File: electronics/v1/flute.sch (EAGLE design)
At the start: 45 parts, among them P1 PRESSURE_SENSOR, Q1 BC550C, Q2 BC550C

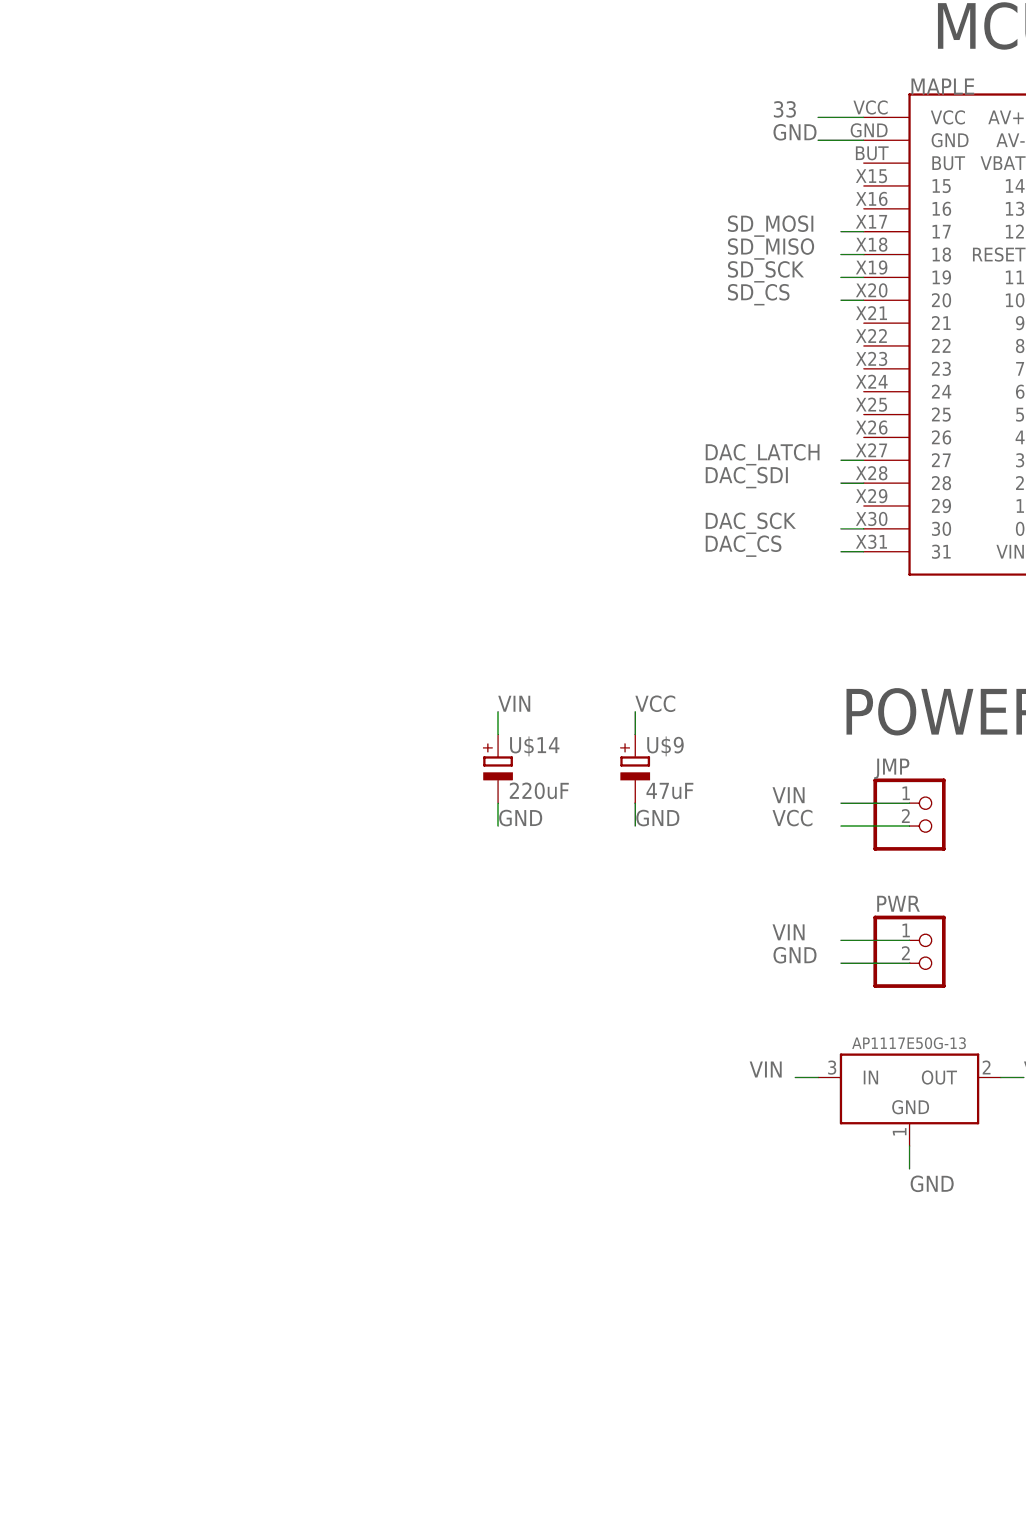
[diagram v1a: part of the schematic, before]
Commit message: Routed V1 (to be checked)
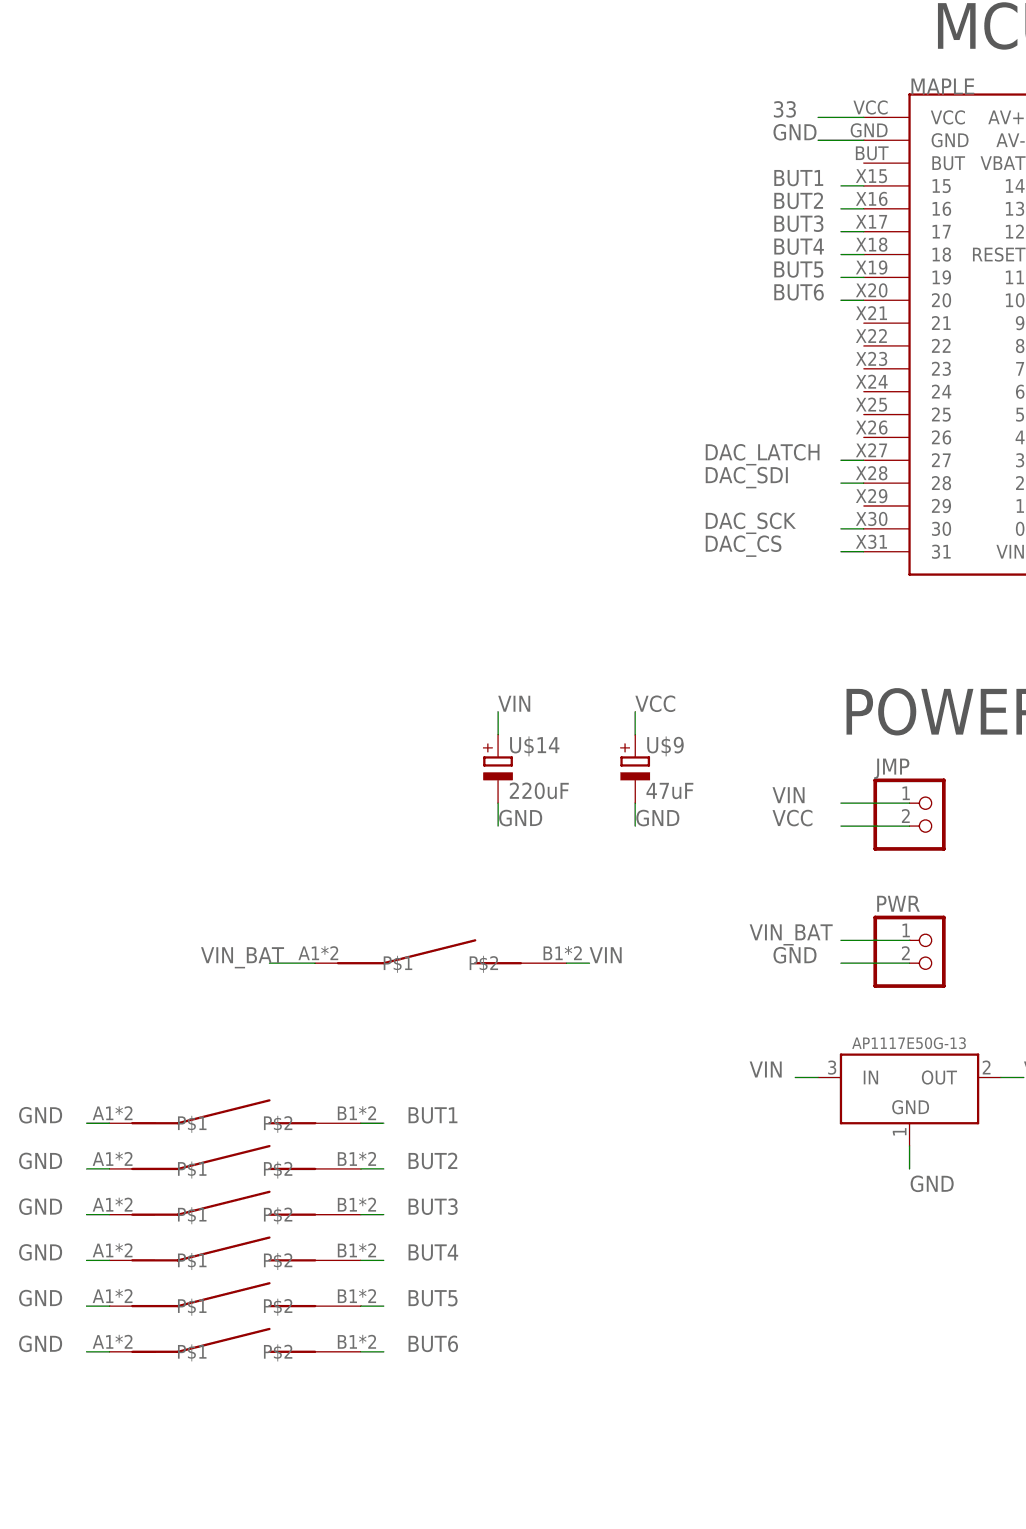
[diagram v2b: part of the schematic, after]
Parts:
- added U$16: SWITCHKCD11, rhoban:SWITCHKCD11
- added U$18, U$19, U$20, U$21, U$22, U$23: SWITCH6X6X10, rhoban:SWITCH6X6X10
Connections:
- removed net SD_CS: MAPLE.20
- removed net SD_MISO: MAPLE.18
- removed net SD_MOSI: MAPLE.17
- removed net SD_SCK: MAPLE.19
- new net BUT1: MAPLE.15, U$18.P$2
- new net BUT2: MAPLE.16, U$19.P$2
- new net BUT3: MAPLE.17, U$20.P$2
- new net BUT4: MAPLE.18, U$21.P$2
- new net BUT5: MAPLE.19, U$22.P$2
- new net BUT6: MAPLE.20, U$23.P$2
- new net VIN_BAT: PWR.1, U$16.P$1
- net GND: now also U$18.P$1, U$19.P$1, U$20.P$1, U$21.P$1, U$22.P$1, U$23.P$1
- net VIN: now also U$16.P$2; no longer PWR.1
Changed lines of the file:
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@@
 <part name="U$9" library="rhoban" deviceset="CPOL_EU" device="PANASONIC_D" value="47uF"/>
 <part name="U$14" library="rhoban" deviceset="CPOL_EU" device="PANASONIC_D8" value="220uF"/>
+<part name="U$16" library="rhoban" deviceset="SWITCH" device="KCD11"/>
+<part name="U$18" library="rhoban" deviceset="SWITCH" device="6X6X10"/>
+<part name="U$19" library="rhoban" deviceset="SWITCH" device="6X6X10"/>
+<part name="U$20" library="rhoban" deviceset="SWITCH" device="6X6X10"/>
+<part name="U$21" library="rhoban" deviceset="SWITCH" device="6X6X10"/>
+<part name="U$22" library="rhoban" deviceset="SWITCH" device="6X6X10"/>
+<part name="U$23" library="rhoban" deviceset="SWITCH" device="6X6X10"/>
 </parts>
 <sheets>
@@
 <instance part="U$9" gate="G$1" x="45.72" y="-38.1"/>
 <instance part="U$14" gate="G$1" x="30.48" y="-38.1"/>
+<instance part="U$16" gate="G$1" x="12.7" y="-58.42"/>
+<instance part="U$18" gate="G$1" x="-10.16" y="-76.2"/>
+<instance part="U$19" gate="G$1" x="-10.16" y="-81.28"/>
+<instance part="U$20" gate="G$1" x="-10.16" y="-86.36"/>
+<instance part="U$21" gate="G$1" x="-10.16" y="-91.44"/>
+<instance part="U$22" gate="G$1" x="-10.16" y="-96.52"/>
+<instance part="U$23" gate="G$1" x="-10.16" y="-101.6"/>
 </instances>
 <busses>
@@
 <label x="30.48" y="-43.18" size="1.778" layer="95"/>
 </segment>
+<segment>
+<pinref part="U$18" gate="G$1" pin="P$1"/>
+<wire x1="-12.7" y1="-76.2" x2="-15.24" y2="-76.2" width="0.1524" layer="91"/>
+<label x="-22.86" y="-76.2" size="1.778" layer="95"/>
+</segment>
+<segment>
+<pinref part="U$19" gate="G$1" pin="P$1"/>
+<wire x1="-12.7" y1="-81.28" x2="-15.24" y2="-81.28" width="0.1524" layer="91"/>
+<label x="-22.86" y="-81.28" size="1.778" layer="95"/>
+</segment>
+<segment>
+<pinref part="U$20" gate="G$1" pin="P$1"/>
+<wire x1="-12.7" y1="-86.36" x2="-15.24" y2="-86.36" width="0.1524" layer="91"/>
+<label x="-22.86" y="-86.36" size="1.778" layer="95"/>
+</segment>
+<segment>
+<pinref part="U$21" gate="G$1" pin="P$1"/>
+<wire x1="-12.7" y1="-91.44" x2="-15.24" y2="-91.44" width="0.1524" layer="91"/>
+<label x="-22.86" y="-91.44" size="1.778" layer="95"/>
+</segment>
+<segment>
+<pinref part="U$22" gate="G$1" pin="P$1"/>
+<wire x1="-12.7" y1="-96.52" x2="-15.24" y2="-96.52" width="0.1524" layer="91"/>
+<label x="-22.86" y="-96.52" size="1.778" layer="95"/>
+</segment>
+<segment>
+<pinref part="U$23" gate="G$1" pin="P$1"/>
+<wire x1="-12.7" y1="-101.6" x2="-15.24" y2="-101.6" width="0.1524" layer="91"/>
+<label x="-22.86" y="-101.6" size="1.778" layer="95"/>
+</segment>
 </net>
 <net name="VCC" class="0">
@@
 </segment>
 <segment>
-<pinref part="PWR" gate="G$1" pin="1"/>
-<wire x1="76.2" y1="-55.88" x2="68.58" y2="-55.88" width="0.1524" layer="91"/>
-<label x="60.96" y="-55.88" size="1.778" layer="95"/>
-</segment>
-<segment>
 <pinref part="U$3" gate="G$1" pin="IN"/>
 <wire x1="66.04" y1="-71.12" x2="63.5" y2="-71.12" width="0.1524" layer="91"/>
@@
 <label x="30.48" y="-30.48" size="1.778" layer="95"/>
 </segment>
+<segment>
+<pinref part="U$16" gate="G$1" pin="P$2"/>
+<wire x1="38.1" y1="-58.42" x2="40.64" y2="-58.42" width="0.1524" layer="91"/>
+<label x="40.64" y="-58.42" size="1.778" layer="95"/>
+</segment>
 </net>
 <net name="AUDIO" class="0">
@@
 <wire x1="71.12" y1="-2.54" x2="68.58" y2="-2.54" width="0.1524" layer="91"/>
 <label x="53.34" y="-2.54" size="1.778" layer="95"/>
-</segment>
-</net>
-<net name="SD_MOSI" class="0">
-<segment>
-<pinref part="MAPLE" gate="G$1" pin="17"/>
-<wire x1="71.12" y1="22.86" x2="68.58" y2="22.86" width="0.1524" layer="91"/>
-<label x="55.88" y="22.86" size="1.778" layer="95"/>
-</segment>
-</net>
-<net name="SD_MISO" class="0">
-<segment>
-<pinref part="MAPLE" gate="G$1" pin="18"/>
-<wire x1="71.12" y1="20.32" x2="68.58" y2="20.32" width="0.1524" layer="91"/>
-<label x="55.88" y="20.32" size="1.778" layer="95"/>
-</segment>
-</net>
-<net name="SD_SCK" class="0">
-<segment>
-<pinref part="MAPLE" gate="G$1" pin="19"/>
-<wire x1="71.12" y1="17.78" x2="68.58" y2="17.78" width="0.1524" layer="91"/>
-<label x="55.88" y="17.78" size="1.778" layer="95"/>
-</segment>
-</net>
-<net name="SD_CS" class="0">
-<segment>
-<pinref part="MAPLE" gate="G$1" pin="20"/>
-<wire x1="71.12" y1="15.24" x2="68.58" y2="15.24" width="0.1524" layer="91"/>
-<label x="55.88" y="15.24" size="1.778" layer="95"/>
 </segment>
 </net>
@@
 </segment>
 </net>
+<net name="VIN_BAT" class="1">
+<segment>
+<pinref part="U$16" gate="G$1" pin="P$1"/>
+<wire x1="10.16" y1="-58.42" x2="5.08" y2="-58.42" width="0.1524" layer="91"/>
+<label x="-2.54" y="-58.42" size="1.778" layer="95"/>
+</segment>
+<segment>
+<pinref part="PWR" gate="G$1" pin="1"/>
+<wire x1="76.2" y1="-55.88" x2="68.58" y2="-55.88" width="0.1524" layer="91"/>
+<label x="58.42" y="-55.88" size="1.778" layer="95"/>
+</segment>
+</net>
+<net name="BUT1" class="0">
+<segment>
+<pinref part="U$18" gate="G$1" pin="P$2"/>
+<wire x1="15.24" y1="-76.2" x2="17.78" y2="-76.2" width="0.1524" layer="91"/>
+<label x="20.32" y="-76.2" size="1.778" layer="95"/>
+</segment>
+<segment>
+<pinref part="MAPLE" gate="G$1" pin="15"/>
+<wire x1="71.12" y1="27.94" x2="68.58" y2="27.94" width="0.1524" layer="91"/>
+<label x="60.96" y="27.94" size="1.778" layer="95"/>
+</segment>
+</net>
+<net name="BUT2" class="0">
+<segment>
+<pinref part="U$19" gate="G$1" pin="P$2"/>
+<wire x1="15.24" y1="-81.28" x2="17.78" y2="-81.28" width="0.1524" layer="91"/>
+<label x="20.32" y="-81.28" size="1.778" layer="95"/>
+</segment>
+<segment>
+<pinref part="MAPLE" gate="G$1" pin="16"/>
+<wire x1="71.12" y1="25.4" x2="68.58" y2="25.4" width="0.1524" layer="91"/>
+<label x="60.96" y="25.4" size="1.778" layer="95"/>
+</segment>
+</net>
+<net name="BUT3" class="0">
+<segment>
+<pinref part="U$20" gate="G$1" pin="P$2"/>
+<wire x1="15.24" y1="-86.36" x2="17.78" y2="-86.36" width="0.1524" layer="91"/>
+<label x="20.32" y="-86.36" size="1.778" layer="95"/>
+</segment>
+<segment>
+<pinref part="MAPLE" gate="G$1" pin="17"/>
+<wire x1="71.12" y1="22.86" x2="68.58" y2="22.86" width="0.1524" layer="91"/>
+<label x="60.96" y="22.86" size="1.778" layer="95"/>
+</segment>
+</net>
+<net name="BUT4" class="0">
+<segment>
+<pinref part="U$21" gate="G$1" pin="P$2"/>
+<wire x1="15.24" y1="-91.44" x2="17.78" y2="-91.44" width="0.1524" layer="91"/>
+<label x="20.32" y="-91.44" size="1.778" layer="95"/>
+</segment>
+<segment>
+<pinref part="MAPLE" gate="G$1" pin="18"/>
+<wire x1="71.12" y1="20.32" x2="68.58" y2="20.32" width="0.1524" layer="91"/>
+<label x="60.96" y="20.32" size="1.778" layer="95"/>
+</segment>
+</net>
+<net name="BUT5" class="0">
+<segment>
+<pinref part="U$22" gate="G$1" pin="P$2"/>
+<wire x1="15.24" y1="-96.52" x2="17.78" y2="-96.52" width="0.1524" layer="91"/>
+<label x="20.32" y="-96.52" size="1.778" layer="95"/>
+</segment>
+<segment>
+<pinref part="MAPLE" gate="G$1" pin="19"/>
+<wire x1="71.12" y1="17.78" x2="68.58" y2="17.78" width="0.1524" layer="91"/>
+<label x="60.96" y="17.78" size="1.778" layer="95"/>
+</segment>
+</net>
+<net name="BUT6" class="0">
+<segment>
+<pinref part="U$23" gate="G$1" pin="P$2"/>
+<wire x1="15.24" y1="-101.6" x2="17.78" y2="-101.6" width="0.1524" layer="91"/>
+<label x="20.32" y="-101.6" size="1.778" layer="95"/>
+</segment>
+<segment>
+<pinref part="MAPLE" gate="G$1" pin="20"/>
+<wire x1="71.12" y1="15.24" x2="68.58" y2="15.24" width="0.1524" layer="91"/>
+<label x="60.96" y="15.24" size="1.778" layer="95"/>
+</segment>
+</net>

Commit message: up
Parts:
- added U$24: HC05, rhoban:HC05
- U$17: value RHOBAN_MCP4822 -> MCP4822
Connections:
- removed net N$16: C1.1, R20.2
- new net KEY: MAPLE.22, U$24.KEY
- new net N$12: C1.2, R20.1
- new net RX1: MAPLE.25, U$24.DOUT
- new net TX1: MAPLE.26, U$24.DIN
- net 33: now also U$24.3.3V
- net GND: now also U$24.GND; no longer R22.2
- net N$18: now also R20.2; no longer C1.2
- net N$20: now also C1.1; no longer R20.1
- net VIN: now also R22.2
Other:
- moved on the sheet: C1, R20
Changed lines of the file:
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@@
 <part name="R1" library="SparkFun-Passives" deviceset="RESISTOR" device="0805-RES" value="10k"/>
 <part name="R2" library="SparkFun-Passives" deviceset="RESISTOR" device="0805-RES" value="10k"/>
-<part name="U$17" library="rhoban" deviceset="RHOBAN_MCP4822" device=""/>
+<part name="U$17" library="rhoban" deviceset="RHOBAN_MCP4822" device="" value="MCP4822"/>
 <part name="P1" library="rhoban" deviceset="PRESSURE_SENSOR" device=""/>
 <part name="AMP" library="rhoban" deviceset="AN7511" device="DIP8"/>
@@
 <part name="U$22" library="rhoban" deviceset="SWITCH" device="6X6X10"/>
 <part name="U$23" library="rhoban" deviceset="SWITCH" device="6X6X10"/>
+<part name="U$24" library="rhoban" deviceset="HC05" device=""/>
 </parts>
 <sheets>
@@
 <instance part="JACK" gate="G$1" x="218.44" y="17.78"/>
 <instance part="R19" gate="G$1" x="208.28" y="30.48" rot="R270"/>
-<instance part="R20" gate="G$1" x="251.46" y="25.4"/>
-<instance part="C1" gate="G$1" x="264.16" y="25.4" rot="R90"/>
+<instance part="R20" gate="G$1" x="261.62" y="25.4"/>
+<instance part="C1" gate="G$1" x="248.92" y="25.4" rot="R90"/>
 <instance part="R21" gate="G$1" x="269.24" y="20.32" rot="R90"/>
 <instance part="GND1" gate="1" x="269.24" y="10.16"/>
@@
 <instance part="U$22" gate="G$1" x="-10.16" y="-96.52"/>
 <instance part="U$23" gate="G$1" x="-10.16" y="-101.6"/>
+<instance part="U$24" gate="G$1" x="33.02" y="27.94"/>
 </instances>
 <busses>
@@
 </segment>
 <segment>
-<pinref part="R22" gate="G$1" pin="2"/>
-<wire x1="284.48" y1="38.1" x2="284.48" y2="40.64" width="0.1524" layer="91"/>
-<label x="284.48" y="40.64" size="1.778" layer="95" rot="R90"/>
-</segment>
-<segment>
 <pinref part="U$3" gate="G$1" pin="GND"/>
 <wire x1="76.2" y1="-78.74" x2="76.2" y2="-81.28" width="0.1524" layer="91"/>
@@
 <wire x1="-12.7" y1="-101.6" x2="-15.24" y2="-101.6" width="0.1524" layer="91"/>
 <label x="-22.86" y="-101.6" size="1.778" layer="95"/>
+</segment>
+<segment>
+<pinref part="U$24" gate="G$1" pin="GND"/>
+<wire x1="20.32" y1="30.48" x2="17.78" y2="30.48" width="0.1524" layer="91"/>
+<label x="10.16" y="30.48" size="1.778" layer="95"/>
 </segment>
 </net>
@@
 <label x="40.64" y="-58.42" size="1.778" layer="95"/>
 </segment>
+<segment>
+<pinref part="R22" gate="G$1" pin="2"/>
+<wire x1="284.48" y1="38.1" x2="284.48" y2="40.64" width="0.1524" layer="91"/>
+<label x="284.48" y="40.64" size="1.778" layer="95" rot="R90"/>
+</segment>
 </net>
 <net name="AUDIO" class="0">
@@
 <wire x1="71.12" y1="35.56" x2="66.04" y2="35.56" width="0.1524" layer="91"/>
 <label x="60.96" y="35.56" size="1.778" layer="95"/>
+</segment>
+<segment>
+<pinref part="U$24" gate="G$1" pin="3.3V"/>
+<wire x1="20.32" y1="33.02" x2="17.78" y2="33.02" width="0.1524" layer="91"/>
+<label x="10.16" y="33.02" size="1.778" layer="95"/>
 </segment>
 </net>
@@
 <wire x1="241.3" y1="25.4" x2="243.84" y2="25.4" width="0.1524" layer="91"/>
 <wire x1="243.84" y1="22.86" x2="243.84" y2="25.4" width="0.1524" layer="91"/>
-<wire x1="243.84" y1="25.4" x2="246.38" y2="25.4" width="0.1524" layer="91"/>
-<pinref part="R20" gate="G$1" pin="1"/>
-</segment>
-</net>
-<net name="N$16" class="0">
-<segment>
+<pinref part="C1" gate="G$1" pin="1"/>
+<junction x="243.84" y="25.4"/>
+</segment>
+</net>
+<net name="N$18" class="0">
+<segment>
+<pinref part="R21" gate="G$1" pin="2"/>
+<pinref part="AMP" gate="G$1" pin="INPUT"/>
+<wire x1="266.7" y1="25.4" x2="289.56" y2="25.4" width="0.1524" layer="91"/>
 <pinref part="R20" gate="G$1" pin="2"/>
-<wire x1="256.54" y1="25.4" x2="259.08" y2="25.4" width="0.1524" layer="91"/>
-<pinref part="C1" gate="G$1" pin="1"/>
-</segment>
-</net>
-<net name="N$18" class="0">
-<segment>
-<pinref part="C1" gate="G$1" pin="2"/>
-<pinref part="R21" gate="G$1" pin="2"/>
+<junction x="266.7" y="25.4"/>
 <wire x1="266.7" y1="25.4" x2="269.24" y2="25.4" width="0.1524" layer="91"/>
-<pinref part="AMP" gate="G$1" pin="INPUT"/>
-<wire x1="269.24" y1="25.4" x2="289.56" y2="25.4" width="0.1524" layer="91"/>
 </segment>
 </net>
@@
 </segment>
 </net>
+<net name="N$12" class="0">
+<segment>
+<pinref part="R20" gate="G$1" pin="1"/>
+<pinref part="C1" gate="G$1" pin="2"/>
+<wire x1="251.46" y1="25.4" x2="256.54" y2="25.4" width="0.1524" layer="91"/>
+</segment>
+</net>
+<net name="RX1" class="0">
+<segment>
+<pinref part="MAPLE" gate="G$1" pin="25"/>
+<wire x1="71.12" y1="2.54" x2="68.58" y2="2.54" width="0.1524" layer="91"/>
+<label x="60.96" y="2.54" size="1.778" layer="95"/>
+</segment>
+<segment>
+<pinref part="U$24" gate="G$1" pin="DOUT"/>
+<wire x1="20.32" y1="25.4" x2="17.78" y2="25.4" width="0.1524" layer="91"/>
+<label x="10.16" y="25.4" size="1.778" layer="95"/>
+</segment>
+</net>
+<net name="TX1" class="0">
+<segment>
+<pinref part="MAPLE" gate="G$1" pin="26"/>
+<wire x1="71.12" y1="0" x2="68.58" y2="0" width="0.1524" layer="91"/>
+<label x="60.96" y="0" size="1.778" layer="95"/>
+</segment>
+<segment>
+<pinref part="U$24" gate="G$1" pin="DIN"/>
+<wire x1="20.32" y1="27.94" x2="17.78" y2="27.94" width="0.1524" layer="91"/>
+<label x="10.16" y="27.94" size="1.778" layer="95"/>
+</segment>
+</net>
+<net name="KEY" class="0">
+<segment>
+<pinref part="MAPLE" gate="G$1" pin="22"/>
+<wire x1="71.12" y1="10.16" x2="68.58" y2="10.16" width="0.1524" layer="91"/>
+<label x="60.96" y="10.16" size="1.778" layer="95"/>
+</segment>
+<segment>
+<pinref part="U$24" gate="G$1" pin="KEY"/>
+<wire x1="20.32" y1="22.86" x2="17.78" y2="22.86" width="0.1524" layer="91"/>
+<label x="10.16" y="22.86" size="1.778" layer="95"/>
+</segment>
+</net>

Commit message: Fixes
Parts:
- R1, R2: value 10k -> 1k
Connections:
- removed net N$6: JACK.GND
- net GND: now also JACK.GND
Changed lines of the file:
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@@
 <part name="Q1" library="transistor-npn" deviceset="BC550*" device="" technology="C"/>
 <part name="Q2" library="transistor-npn" deviceset="BC550*" device="" technology="C"/>
-<part name="R1" library="SparkFun-Passives" deviceset="RESISTOR" device="0805-RES" value="10k"/>
-<part name="R2" library="SparkFun-Passives" deviceset="RESISTOR" device="0805-RES" value="10k"/>
+<part name="R1" library="SparkFun-Passives" deviceset="RESISTOR" device="0805-RES" value="1k"/>
+<part name="R2" library="SparkFun-Passives" deviceset="RESISTOR" device="0805-RES" value="1k"/>
 <part name="U$17" library="rhoban" deviceset="RHOBAN_MCP4822" device="" value="MCP4822"/>
 <part name="P1" library="rhoban" deviceset="PRESSURE_SENSOR" device=""/>
@@
 <label x="10.16" y="30.48" size="1.778" layer="95"/>
 </segment>
+<segment>
+<pinref part="JACK" gate="G$1" pin="GND"/>
+<wire x1="213.36" y1="20.32" x2="210.82" y2="20.32" width="0.1524" layer="91"/>
+<wire x1="210.82" y1="20.32" x2="210.82" y2="17.78" width="0.1524" layer="91"/>
+<label x="210.82" y="15.24" size="1.778" layer="95"/>
+</segment>
 </net>
 <net name="VCC" class="0">
@@
 </segment>
 </net>
-<net name="N$6" class="0">
-<segment>
-<pinref part="JACK" gate="G$1" pin="GND"/>
-<wire x1="213.36" y1="20.32" x2="210.82" y2="20.32" width="0.1524" layer="91"/>
-<wire x1="210.82" y1="20.32" x2="210.82" y2="17.78" width="0.1524" layer="91"/>
-</segment>
-</net>
